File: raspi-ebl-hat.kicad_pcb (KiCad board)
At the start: 2 copper layers, 3 parts, among them J1 43045-1012, J2 43650-0515, J3 43650-0615

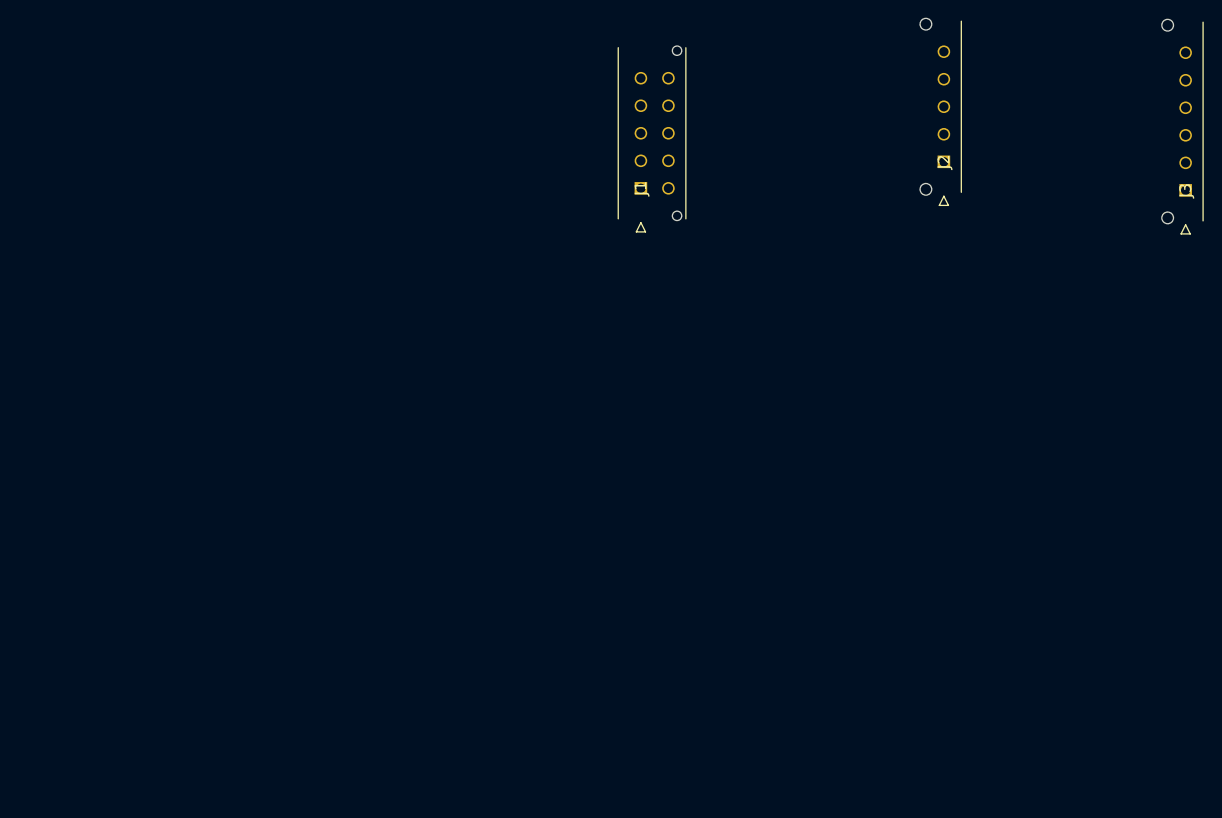
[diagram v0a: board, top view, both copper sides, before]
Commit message: imported pihat-template stuff
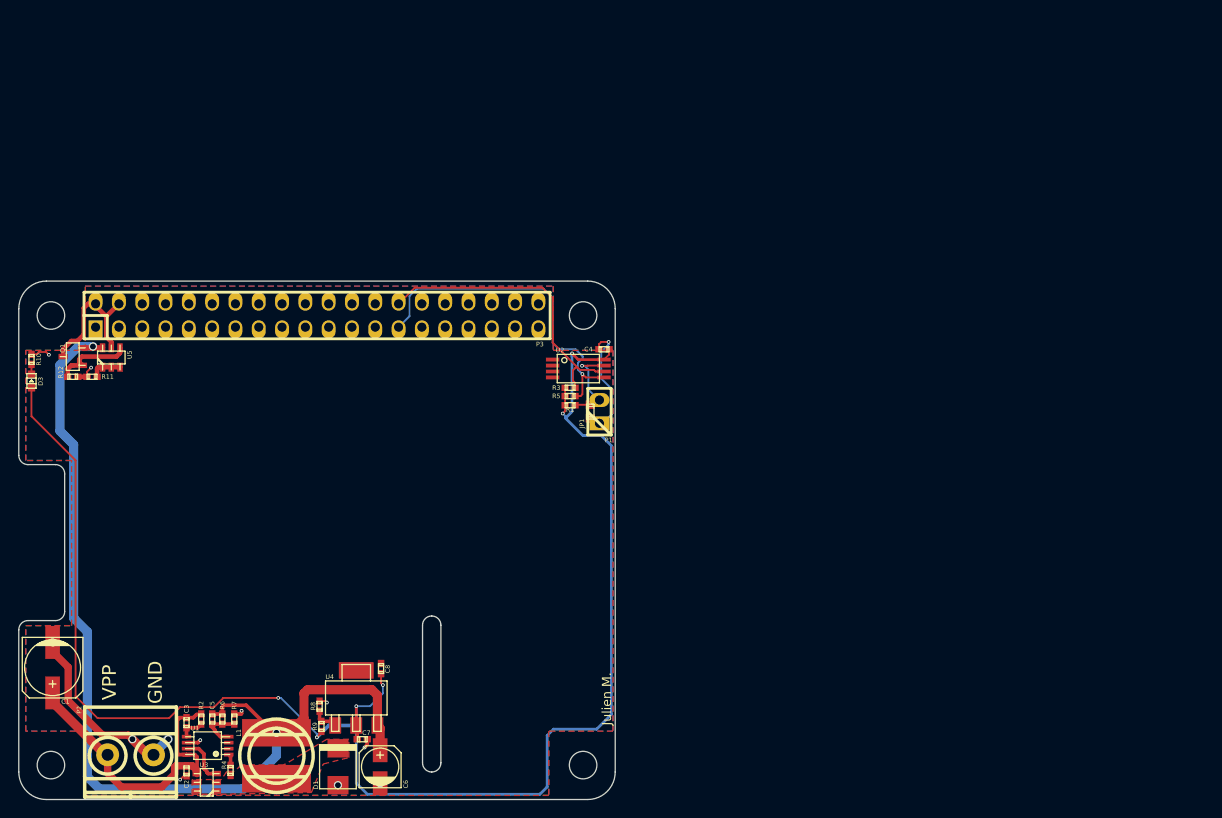
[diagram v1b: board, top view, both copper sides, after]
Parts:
- removed J1: 43045-1012, parts:43045-10YY_12,13,14
- removed J2: 43650-0515, parts:43650-05YY_15,16,17
- removed J3: 43650-0615, parts:43650-06YY_15,16,17
- added C1: 50uf/50v, w_smd_cap:c_elec_6.3x7.7, F.Cu at (108.6, 113.2)
- added C2: 0.1uf, w_smd_cap:c_0402, F.Cu at (123.2, 124.4)
- added C3: 1nf, w_smd_cap:c_0402, F.Cu at (123.2, 119.2)
- added C4: 0.1uf, w_smd_cap:c_0402, F.Cu at (168.7, 78.5)
- added C5: 0.1uf, w_smd_cap:c_0402, F.Cu at (126.0, 118.8)
- added C6: 10uf/6.3V, w_smd_cap:c_elec_4x5.3, F.Cu at (144.3, 124.0)
- added C7: 0.1uf, w_smd_cap:c_0402, F.Cu at (142.3, 121.0)
- added C8: 1uf, w_smd_cap:c_0402, F.Cu at (144.4, 113.3)
- added D1: DIODESCH, w_smd_diode:do214aa, F.Cu at (139.7, 124.0)
- added D3: LED, w_smd_leds:Led_0603, F.Cu at (106.3, 81.9)
- added JP1: JUMPER, w_smd_resistors:r_0603, F.Cu at (167.2, 85.3)
- added L1: 22uH, w_smd_inductors:inductor_smd_8x5mm, F.Cu at (133.0, 122.8)
- added P1: CONN_01X02, w_pin_strip:pin_strip_2, F.Cu at (168.2, 85.3)
- added P2: CONN_01X02, w_conn_mkds:mkds_1,5-2, F.Cu at (117.1, 122.7)
- added P3: Raspberry_Pi_+_Conn, w_pin_strip:pin_socket_20x2, F.Cu at (137.4, 74.8)
- added Q1: BSS138, w_smd_trans:sot23, F.Cu at (110.8, 79.3)
- added R1: 1k, w_smd_resistors:r_0402, F.Cu at (165.0, 84.6)
- added R10: 360, w_smd_resistors:r_0402, F.Cu at (106.3, 79.6)
- added R11: 10k, w_smd_resistors:r_0402, F.Cu at (112.9, 81.5)
- added R12: 47k, w_smd_resistors:r_0402, F.Cu at (110.8, 81.5)
- added R2: 24k, w_smd_resistors:r_0402, F.Cu at (124.8, 118.8)
- added R3: 3.9k, w_smd_resistors:r_0402, F.Cu at (165.0, 82.7)
- added R4: 270, w_smd_resistors:r_0402, F.Cu at (128.0, 124.4)
- added R5: 3.9k, w_smd_resistors:r_0402, F.Cu at (165.0, 83.6)
- added R6: 30k, w_smd_resistors:r_0402, F.Cu at (127.1, 118.8)
- added R7: 10k, w_smd_resistors:r_0402, F.Cu at (128.4, 118.8)
- added R8: 390, w_smd_resistors:r_0402, F.Cu at (137.7, 117.4)
- added R9: 240, w_smd_resistors:r_0402, F.Cu at (137.9, 119.6)
- added REF**: MountingHole_3mm, Mounting_Holes:MountingHole_3mm, F.Cu at (166.4, 74.8)
- added REF**: MountingHole_3mm, Mounting_Holes:MountingHole_3mm, F.Cu at (108.4, 74.8)
- added REF**: MountingHole_3mm, Mounting_Holes:MountingHole_3mm, F.Cu at (108.4, 123.8)
- added REF**: MountingHole_3mm, Mounting_Holes:MountingHole_3mm, F.Cu at (166.4, 123.8)
- added U1: LM3489, w_smd_dil:msoic-8, F.Cu at (125.5, 121.7)
- added U2: CAT24C32HU4I-GT3, w_smd_dil:tssop-8, F.Cu at (165.9, 80.6)
- added U3: FDC5614P, w_smd_trans:sot23-6, F.Cu at (125.4, 125.7)
- added U4: LM1117IMPX-ADJ, w_smd_trans:sot223, F.Cu at (141.7, 116.5)
- added U5: DMMT5401, w_smd_trans:sot23-6, F.Cu at (115.0, 79.4)
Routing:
- net +3V3: track 0.00 -> 176.1 mm, vias 0 -> 6
- net +5V: track 0.00 -> 108.0 mm, vias 0 -> 2
- net GND: track 0.00 -> 44.4 mm, vias 0 -> 13
- net Net-(P3-Pad27): track 0.00 -> 36.9 mm, vias 0 -> 1
- net +24V: track 0.00 -> 35.0 mm
- net Net-(P3-Pad28): track 0.00 -> 32.4 mm
- net /Back Power Protection/5V_MCU: track 0.00 -> 15.5 mm
- net Net-(JP1-Pad1): track 0.00 -> 10.0 mm, vias 0 -> 1
- net Net-(Q1-Pad1): track 0.00 -> 8.73 mm
- net Net-(U1-Pad7): track 0.00 -> 5.38 mm
- net Net-(C5-Pad2): track 0.00 -> 5.06 mm
- net Net-(R11-Pad1): track 0.00 -> 3.44 mm
- net Net-(R8-Pad1): track 0.00 -> 2.87 mm
- net Net-(C3-Pad2): track 0.00 -> 2.74 mm
- net Net-(R4-Pad2): track 0.00 -> 1.26 mm
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- added copper zone on B.Cu, net GND
- added copper zone on F.Cu, net GND
- added copper zone on F.Cu, net Net-(D1-Pad2)
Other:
- board outline added: 65 x 56.5 mm
- board text added: "CERN OHL V1.2"
- board text added: "GND"
- board text added: "Julien M."
- board text added: "VPP"

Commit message: added EBL header
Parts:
- added J101: 43045-1012, raspi-ebl-hat:43045-10YY_12,13,14, F.Cu at (143.3, 104.3)
- added J102: 43650-0515, raspi-ebl-hat:43650-05YY_15,16,17, F.Cu at (143.4, 93.8)
- added J103: 43650-0615, raspi-ebl-hat:43650-06YY_15,16,17, F.Cu at (146.4, 86.3)
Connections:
- U1 pad 3: Net-(U1-Pad3) -> unconnected-(U1-Pad3)
